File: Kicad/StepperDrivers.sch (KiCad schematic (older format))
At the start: 36 parts, among them J3 ZAXIS, J4 XAXIS, J5 YAXIS, U4 TMC2130-TA, U5 TMC2130-TA, U6 TMC2130-TA

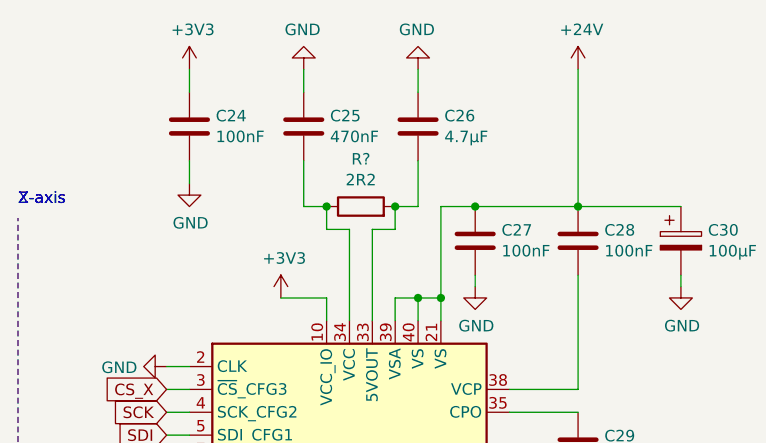
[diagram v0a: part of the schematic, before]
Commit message: Completed the TMC2130 layout and Boost converter layout
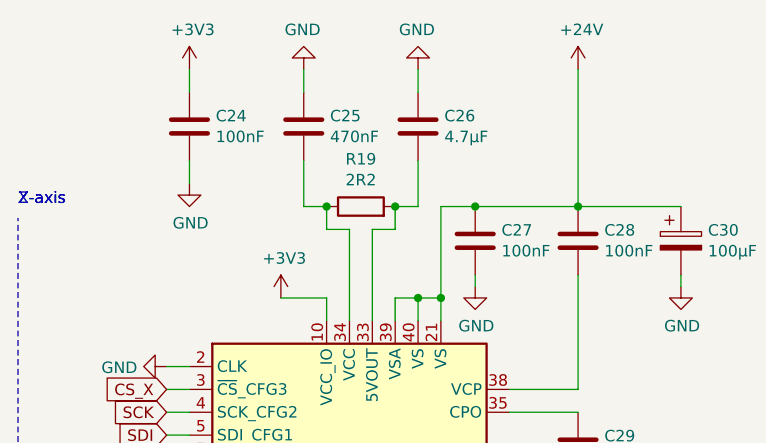
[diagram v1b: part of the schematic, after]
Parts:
- gave numbers to parts that had none: 1
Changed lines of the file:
@@
 	2450 5450 2450 5350
 $Comp
-L Device:R R?
+L Device:R R19
 U 1 1 5E2CA26C
 P 2500 2450
-F 0 "R?" V 2707 2450 50  0000 C CNN
+F 0 "R19" V 2707 2450 50  0000 C CNN
 F 1 "2R2" V 2616 2450 50  0000 C CNN
 F 2 "Resistor_SMD:R_0603_1608Metric" V 2430 2450 50  0001 C CNN
